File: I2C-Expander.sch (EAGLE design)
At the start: 79 parts, among them IC1 MCP23017SO, IC2 PCA9555D, Q0 P-FET, Q1 P-FET, Q10 P-FET, Q11 P-FET, Q12 P-FET, Q13 P-FET, Q14 P-FET, Q15 P-FET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

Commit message: added LED on input changed interrupt pins
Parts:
- added LED17: GREEN, SPCoast:LED0603-LED
- added R23: 2K2, SPCoast:R0603-RES
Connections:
- new net N$19: LED17.C, R23.1
- net !INT: now also R23.2
- net VCC: now also LED17.A
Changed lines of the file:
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@@
 <part name="P+25" library="supply1" deviceset="VCC" device=""/>
 <part name="GND2" library="SPCoast" deviceset="GND" device=""/>
+<part name="R23" library="SPCoast" deviceset="R*" device="0603-RES" value="2K2"/>
+<part name="LED17" library="SPCoast" deviceset="LED*" device="0603-LED" value="GREEN"/>
 </parts>
 <sheets>
@@
 </instance>
 <instance part="GND2" gate="1" x="43.18" y="88.9"/>
+<instance part="R23" gate="R" x="106.68" y="12.7" smashed="yes" rot="MR270">
+<attribute name="NAME" x="107.95" y="19.8374" size="1.778" layer="95" rot="MR180"/>
+<attribute name="VALUE" x="109.982" y="16.51" size="1.016" layer="96" rot="MR270"/>
+</instance>
+<instance part="LED17" gate="LED" x="106.68" y="22.86"/>
 </instances>
 <busses>
@@
 <segment>
 <wire x1="76.2" y1="15.24" x2="76.2" y2="27.94" width="0.1524" layer="91"/>
-<wire x1="76.2" y1="27.94" x2="68.58" y2="27.94" width="0.1524" layer="91"/>
-<wire x1="68.58" y1="27.94" x2="67.31" y2="27.94" width="0.1524" layer="91"/>
+<wire x1="76.2" y1="27.94" x2="67.31" y2="27.94" width="0.1524" layer="91"/>
 <wire x1="76.2" y1="27.94" x2="76.2" y2="30.48" width="0.1524" layer="91"/>
 <junction x="76.2" y="27.94"/>
@@
 <wire x1="83.82" y1="15.24" x2="83.82" y2="27.94" width="0.1524" layer="91"/>
 <junction x="83.82" y="27.94"/>
+<pinref part="LED17" gate="LED" pin="A"/>
+<wire x1="93.98" y1="27.94" x2="106.68" y2="27.94" width="0.1524" layer="91"/>
+<junction x="93.98" y="27.94"/>
 </segment>
 <segment>
@@
 <pinref part="IC2" gate="G$1" pin="!INT"/>
 </segment>
-</net>
+<segment>
+<pinref part="R23" gate="R" pin="2"/>
+<wire x1="106.68" y1="7.62" x2="106.68" y2="5.08" width="0.1524" layer="91"/>
+<label x="106.68" y="5.08" size="1.016" layer="95" xref="yes"/>
+</segment>
+</net>
+<net name="N$19" class="0">
+<segment>
+<pinref part="LED17" gate="LED" pin="C"/>
+<pinref part="R23" gate="R" pin="1"/>
+<wire x1="106.68" y1="20.32" x2="106.68" y2="17.78" width="0.1524" layer="91"/>
+</segment>
+</net>

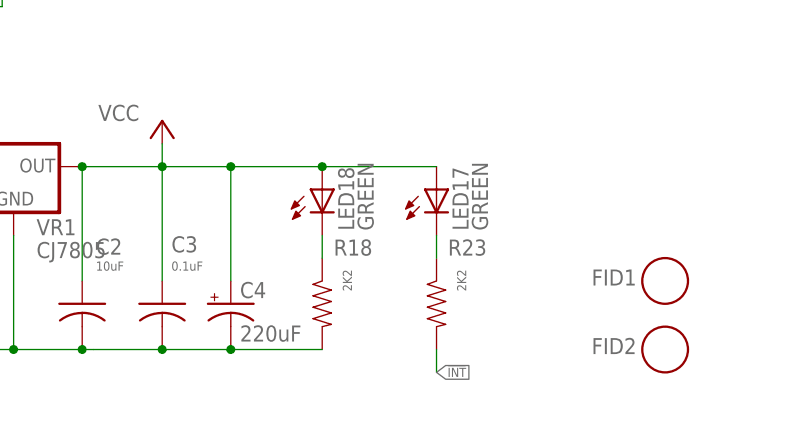
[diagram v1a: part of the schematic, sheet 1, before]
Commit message: fixed SPCoast lbr part orientation
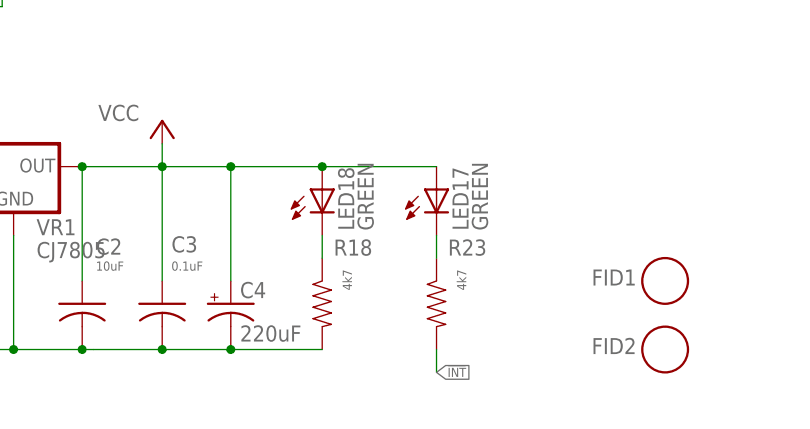
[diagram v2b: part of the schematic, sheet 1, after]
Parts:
- R18, R23: value 2K2 -> 4k7
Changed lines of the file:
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@@
 <layer number="255" name="routoute" color="7" fill="1" visible="no" active="no"/>
 </layers>
-<schematic xreflabel="%F%N" xrefpart="/%S.%C%R">
+<schematic xreflabel="%F%N/%S.%C%R" xrefpart="/%S.%C%R">
 <attributes>
 </attributes>
@@
 <part name="VR1" library="SPCoast" deviceset="VREG-?-*" device="DPAK" technology="5" value="CJ7805"/>
 <part name="P+1" library="supply1" deviceset="VCC" device=""/>
-<part name="R18" library="SPCoast" deviceset="R*" device="0603-RES" value="2K2"/>
+<part name="R18" library="SPCoast" deviceset="R*" device="0603-RES" value="4k7"/>
 <part name="LED18" library="SPCoast" deviceset="LED*" device="0603-LED" value="GREEN"/>
 <part name="SUPPLY2" library="supply2" deviceset="+9V" device=""/>
@@
 <part name="P+25" library="supply1" deviceset="VCC" device=""/>
 <part name="GND2" library="SPCoast" deviceset="GND" device=""/>
-<part name="R23" library="SPCoast" deviceset="R*" device="0603-RES" value="2K2"/>
+<part name="R23" library="SPCoast" deviceset="R*" device="0603-RES" value="4k7"/>
 <part name="LED17" library="SPCoast" deviceset="LED*" device="0603-LED" value="GREEN"/>
 </parts>

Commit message: FID placement & names
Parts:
- U$1, U$2, U$3: value CONNECTOR-IO4-IOBBARE -> CONNECTOR-IO4-IOBNOBSILK; device SPCoast:CONNECTOR-IO4-IOBBARE -> SPCoast:CONNECTOR-IO4-IOBNOBSILK
- U$4: value CONNECTOR-IO4-IOBBARE -> CONNECTOR-IO4-IOBFULL; device SPCoast:CONNECTOR-IO4-IOBBARE -> SPCoast:CONNECTOR-IO4-IOBFULL
- renumbered FID1 to FID-UL, FID2 to FID-LR
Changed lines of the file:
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@@
 <grid distance="100" unitdist="mil" unit="mil" style="dots" multiple="1" display="yes" altdistance="50" altunitdist="mil" altunit="mil"/>
 <layers>
-<layer number="1" name="Top" color="4" fill="1" visible="no" active="no"/>
-<layer number="16" name="Bottom" color="2" fill="1" visible="no" active="no"/>
-<layer number="17" name="Pads" color="23" fill="1" visible="no" active="no"/>
-<layer number="18" name="Vias" color="29" fill="1" visible="no" active="no"/>
-<layer number="19" name="Unrouted" color="6" fill="1" visible="no" active="no"/>
-<layer number="20" name="Dimension" color="15" fill="1" visible="no" active="no"/>
-<layer number="21" name="tPlace" color="19" fill="1" visible="no" active="no"/>
-<layer number="22" name="bPlace" color="17" fill="1" visible="no" active="no"/>
-<layer number="23" name="tOrigins" color="30" fill="1" visible="no" active="no"/>
-<layer number="24" name="bOrigins" color="15" fill="1" visible="no" active="no"/>
-<layer number="25" name="tNames" color="63" fill="1" visible="no" active="no"/>
-<layer number="26" name="bNames" color="34" fill="1" visible="no" active="no"/>
-<layer number="27" name="tValues" color="56" fill="1" visible="no" active="no"/>
-<layer number="28" name="bValues" color="7" fill="1" visible="no" active="no"/>
+<layer number="1" name="Top" color="4" fill="1" visible="yes" active="no"/>
+<layer number="16" name="Bottom" color="2" fill="1" visible="yes" active="no"/>
+<layer number="17" name="Pads" color="23" fill="1" visible="yes" active="no"/>
+<layer number="18" name="Vias" color="29" fill="1" visible="yes" active="no"/>
+<layer number="19" name="Unrouted" color="6" fill="1" visible="yes" active="no"/>
+<layer number="20" name="Dimension" color="15" fill="1" visible="yes" active="no"/>
+<layer number="21" name="tPlace" color="19" fill="1" visible="yes" active="no"/>
+<layer number="22" name="bPlace" color="17" fill="1" visible="yes" active="no"/>
+<layer number="23" name="tOrigins" color="30" fill="1" visible="yes" active="no"/>
+<layer number="24" name="bOrigins" color="15" fill="1" visible="yes" active="no"/>
+<layer number="25" name="tNames" color="63" fill="1" visible="yes" active="no"/>
+<layer number="26" name="bNames" color="34" fill="1" visible="yes" active="no"/>
+<layer number="27" name="tValues" color="56" fill="1" visible="yes" active="no"/>
+<layer number="28" name="bValues" color="7" fill="1" visible="yes" active="no"/>
 <layer number="29" name="tStop" color="7" fill="3" visible="no" active="no"/>
 <layer number="30" name="bStop" color="7" fill="6" visible="no" active="no"/>
@@
 <layer number="35" name="tGlue" color="7" fill="4" visible="no" active="no"/>
 <layer number="36" name="bGlue" color="7" fill="5" visible="no" active="no"/>
-<layer number="37" name="tTest" color="7" fill="1" visible="no" active="no"/>
-<layer number="38" name="bTest" color="7" fill="1" visible="no" active="no"/>
+<layer number="37" name="tTest" color="7" fill="1" visible="yes" active="no"/>
+<layer number="38" name="bTest" color="7" fill="1" visible="yes" active="no"/>
 <layer number="39" name="tKeepout" color="4" fill="11" visible="no" active="no"/>
 <layer number="40" name="bKeepout" color="3" fill="11" visible="no" active="no"/>
@@
 <layer number="44" name="Drills" color="16" fill="1" visible="no" active="no"/>
 <layer number="45" name="Holes" color="35" fill="1" visible="no" active="no"/>
-<layer number="46" name="Milling" color="35" fill="1" visible="no" active="no"/>
-<layer number="47" name="Measures" color="21" fill="1" visible="no" active="no"/>
-<layer number="48" name="Document" color="57" fill="1" visible="no" active="no"/>
-<layer number="49" name="Reference" color="48" fill="1" visible="no" active="no"/>
-<layer number="50" name="dxf" color="7" fill="1" visible="no" active="no"/>
-<layer number="51" name="tDocu" color="24" fill="1" visible="no" active="no"/>
-<layer number="52" name="bDocu" color="7" fill="1" visible="no" active="no"/>
+<layer number="46" name="Milling" color="35" fill="1" visible="yes" active="no"/>
+<layer number="47" name="Measures" color="21" fill="1" visible="yes" active="no"/>
+<layer number="48" name="Document" color="57" fill="1" visible="yes" active="no"/>
+<layer number="49" name="Reference" color="48" fill="1" visible="yes" active="no"/>
+<layer number="50" name="dxf" color="7" fill="1" visible="yes" active="no"/>
+<layer number="51" name="tDocu" color="24" fill="1" visible="yes" active="no"/>
+<layer number="52" name="bDocu" color="7" fill="1" visible="yes" active="no"/>
 <layer number="91" name="Nets" color="2" fill="1" visible="yes" active="yes"/>
 <layer number="92" name="Busses" color="1" fill="1" visible="yes" active="yes"/>
@@
 <layer number="99" name="Anatomie" color="7" fill="1" visible="yes" active="yes"/>
 <layer number="101" name="Hidden" color="57" fill="4" visible="yes" active="yes"/>
-<layer number="2" name="Route2" color="1" fill="3" visible="no" active="no"/>
-<layer number="3" name="Route3" color="4" fill="3" visible="no" active="no"/>
-<layer number="14" name="Route14" color="1" fill="6" visible="no" active="no"/>
-<layer number="15" name="Route15" color="4" fill="6" visible="no" active="no"/>
-<layer number="53" name="tGND_GNDA" color="7" fill="9" visible="no" active="no"/>
-<layer number="54" name="bGND_GNDA" color="1" fill="9" visible="no" active="no"/>
-<layer number="56" name="wert" color="7" fill="1" visible="no" active="no"/>
-<layer number="57" name="tCAD" color="7" fill="1" visible="no" active="no"/>
-<layer number="59" name="tCarbon" color="7" fill="1" visible="no" active="no"/>
-<layer number="60" name="bCarbon" color="7" fill="1" visible="no" active="no"/>
+<layer number="2" name="Route2" color="1" fill="3" visible="yes" active="no"/>
+<layer number="3" name="Route3" color="4" fill="3" visible="yes" active="no"/>
+<layer number="14" name="Route14" color="1" fill="6" visible="yes" active="no"/>
+<layer number="15" name="Route15" color="4" fill="6" visible="yes" active="no"/>
+<layer number="53" name="tGND_GNDA" color="7" fill="9" visible="yes" active="no"/>
+<layer number="54" name="bGND_GNDA" color="1" fill="9" visible="yes" active="no"/>
+<layer number="56" name="wert" color="7" fill="1" visible="yes" active="no"/>
+<layer number="57" name="tCAD" color="7" fill="1" visible="yes" active="no"/>
+<layer number="59" name="tCarbon" color="7" fill="1" visible="yes" active="no"/>
+<layer number="60" name="bCarbon" color="7" fill="1" visible="yes" active="no"/>
 <layer number="90" name="Modules" color="5" fill="1" visible="no" active="no"/>
 <layer number="100" name="Muster" color="7" fill="1" visible="no" active="no"/>
@@
 <part name="OSHW1" library="SPCoast" deviceset="DOC-OSHW-LOGO-" device="M"/>
 <part name="BOARD1" library="SPCoast" deviceset="BOARD" device="80X100-IOB" value="BOARD80X100-IOB"/>
-<part name="FID2" library="SPCoast" deviceset="FIDUCIAL" device=""/>
-<part name="FID1" library="SPCoast" deviceset="FIDUCIAL" device=""/>
+<part name="FID-LR" library="SPCoast" deviceset="FIDUCIAL" device=""/>
+<part name="FID-UL" library="SPCoast" deviceset="FIDUCIAL" device=""/>
 <part name="IC1" library="SPCoast" deviceset="MCP23017" device="SO"/>
 <part name="CON1" library="SPCoast" deviceset="CONNECTOR-I2C" device="LEFT"/>
@@
 <part name="SUPPLY4" library="supply2" deviceset="+9V" device=""/>
 <part name="P+4" library="supply1" deviceset="VCC" device=""/>
-<part name="U$1" library="SPCoast" deviceset="CONNECTOR-IO4-IOB" device="BARE" value="CONNECTOR-IO4-IOBBARE"/>
-<part name="U$2" library="SPCoast" deviceset="CONNECTOR-IO4-IOB" device="BARE" value="CONNECTOR-IO4-IOBBARE"/>
-<part name="U$3" library="SPCoast" deviceset="CONNECTOR-IO4-IOB" device="BARE" value="CONNECTOR-IO4-IOBBARE"/>
-<part name="U$4" library="SPCoast" deviceset="CONNECTOR-IO4-IOB" device="BARE" value="CONNECTOR-IO4-IOBBARE"/>
+<part name="U$1" library="SPCoast" deviceset="CONNECTOR-IO4-IOB" device="NOBSILK" value="CONNECTOR-IO4-IOBNOBSILK"/>
+<part name="U$2" library="SPCoast" deviceset="CONNECTOR-IO4-IOB" device="NOBSILK" value="CONNECTOR-IO4-IOBNOBSILK"/>
+<part name="U$3" library="SPCoast" deviceset="CONNECTOR-IO4-IOB" device="NOBSILK" value="CONNECTOR-IO4-IOBNOBSILK"/>
+<part name="U$4" library="SPCoast" deviceset="CONNECTOR-IO4-IOB" device="FULL" value="CONNECTOR-IO4-IOBFULL"/>
 <part name="SUPPLY3" library="supply2" deviceset="+9V" device=""/>
 <part name="SUPPLY8" library="supply2" deviceset="+9V" device=""/>
@@
 <instance part="OSHW1" gate="DOC-OSHW-LOGO" x="233.68" y="38.1"/>
 <instance part="BOARD1" gate="B" x="210.82" y="33.02"/>
-<instance part="FID2" gate="FID1" x="132.08" y="7.62"/>
-<instance part="FID1" gate="FID1" x="132.08" y="15.24"/>
+<instance part="FID-LR" gate="FID1" x="132.08" y="7.62"/>
+<instance part="FID-UL" gate="FID1" x="132.08" y="15.24"/>
 <instance part="IC1" gate="G$1" x="121.92" y="121.92"/>
 <instance part="CON1" gate="I2C" x="17.78" y="170.18"/>
